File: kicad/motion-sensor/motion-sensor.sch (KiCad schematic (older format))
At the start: 21 parts, among them CON1 BARREL_JACK, IC1 ATMEGA328P-A, P1 ISP, P2 ESP8266, P3 CONN_01X03, P4 CONN_01X03, P5 CONN_01X02, Q1 Q_NMOS_DGS, SW1 Motion-Sensor-1, SW2 Motion-Sensor-2, U1 LM2574HVH-3.3

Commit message: added component lines + enclosure infos
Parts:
- added C1: 100nF, Capacitors_SMD:C_1206_HandSoldering, symbol C
- renumbered C3 to C2
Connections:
- net +3V3: now also C1.1
- net GND: now also C1.2
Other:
- note added: "Anschluss Bewegungsmelder"
- note added: "Mosfet Treiber für PWM"
- note added: "Status LED"
- note added: "Step Down Converter"
- moved on the sheet: D2, R3

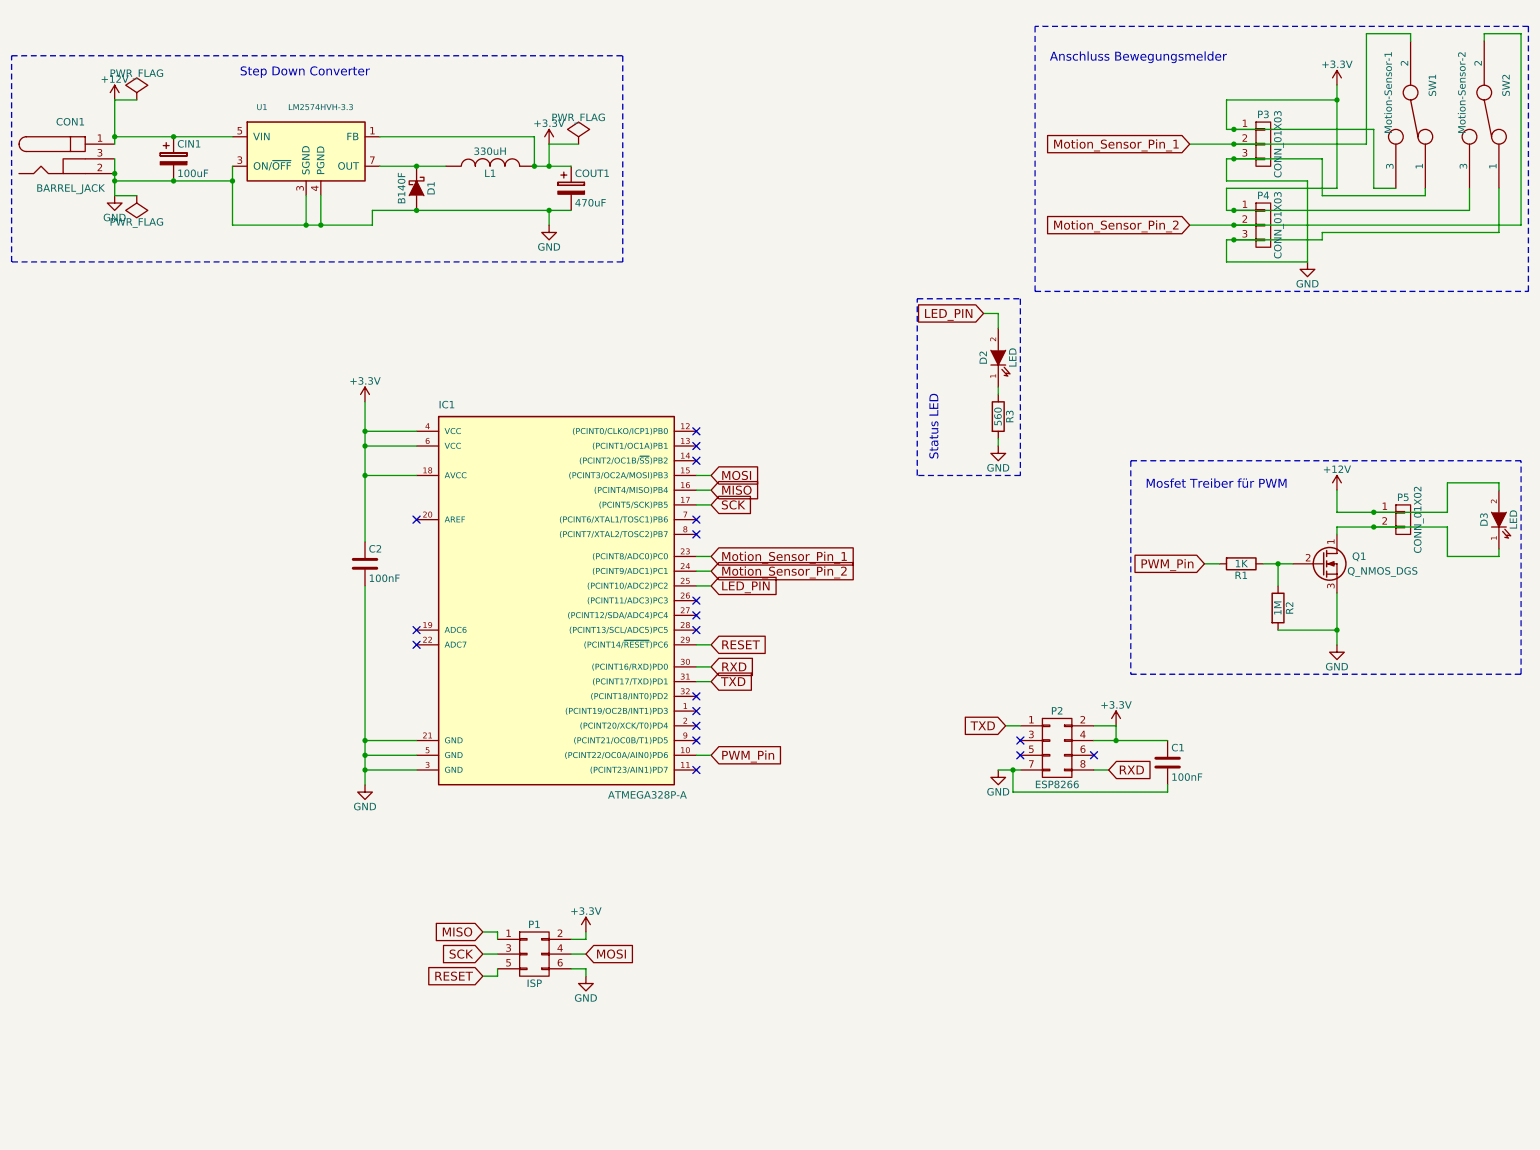
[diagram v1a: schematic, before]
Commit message: added custom footprints and finished schematic
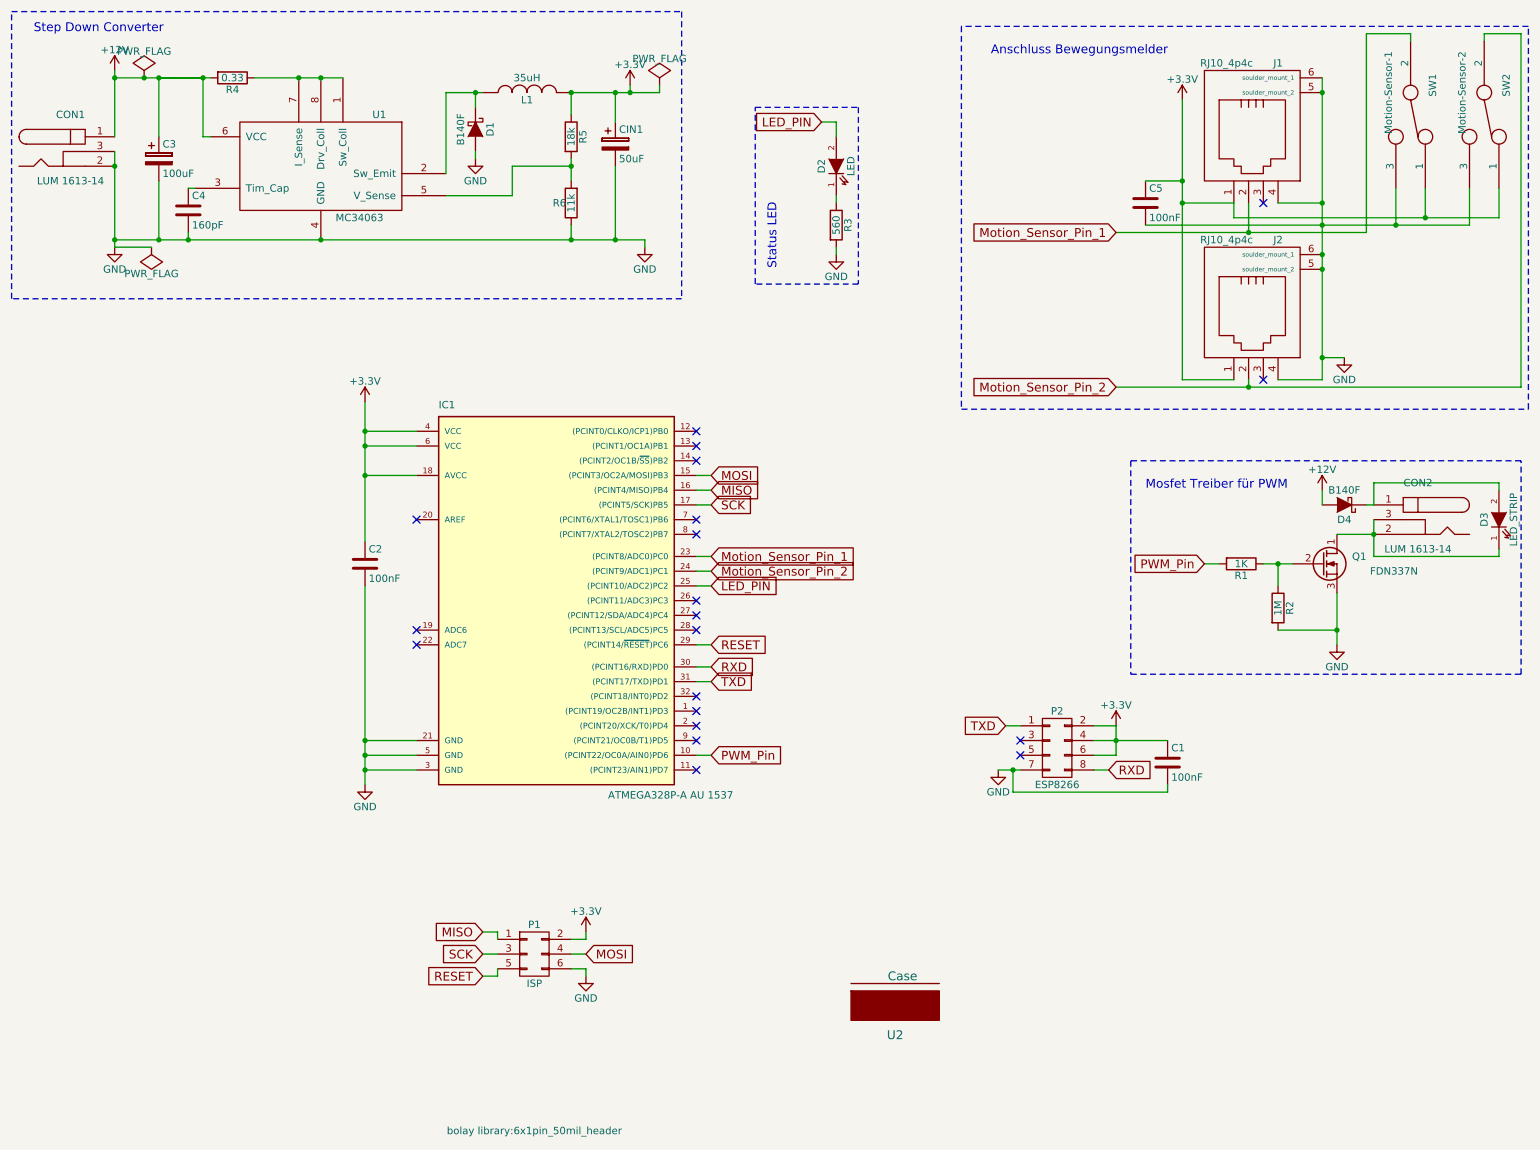
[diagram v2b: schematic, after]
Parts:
- removed P3, P4: CONN_01X03, symbol CONN_01X03
- removed P5: CONN_01X02, symbol CONN_01X02
- removed U1: LM2574HVH-3.3, symbol LM2574HVH-3.3
- added C4: 160pF, Capacitors_SMD:C_1206_HandSoldering, symbol C
- added C5: 100nF, Capacitors_SMD:C_1206_HandSoldering, symbol C
- added CON2: LUM 1613-14, bolay library:barrel_jack_ds_1613_14, symbol BARREL_JACK
- added D4: B140F, Diodes_SMD:DO-214AB_Handsoldering, symbol D_Schottky
- added J1, J2: RJ10_4p4c, bolay library:RJ10_SMD_4p4c, symbol RJ10_4p4c
- added R4: 0.33, Resistors_SMD:R_1206_HandSoldering, symbol R
- added R5: 18k, Resistors_SMD:R_1206_HandSoldering, symbol R
- added R6: 11k, Resistors_SMD:R_1206_HandSoldering, symbol R
- added U1: MC34063, SMD_Packages:SOIC-8-N, symbol MC34063-RESCUE-motion-sensor
- added U2: Case, symbol Case
- C1, C2: Digi-Key (none) -> 1276-2854-1-ND
- C3: renamed from COUT1; value 470uF -> 100uF; footprint Capacitors_SMD:c_elec_6.3x5.8 -> Capacitors_SMD:c_elec_6.3x7.7; Digi-Key (none) -> vorhanden
- CIN1: value 100uF -> 50uF; footprint Capacitors_SMD:c_elec_4x5.8 -> Capacitors_SMD:c_elec_6.3x7.7; Bemerkungen (none) -> 100uF Kondens von reichelt; Digi-Key (none) -> vorhanden
- CON1: value BARREL_JACK -> LUM 1613-14; footprint (none) -> bolay library:barrel_jack_ds_1613_14; Digi-Key (none) -> vorhanden
- D1: footprint (none) -> Diodes_SMD:DO-214AB_Handsoldering; Digi-Key (none) -> vorhanden
- D2: footprint (none) -> LEDs:LED-1206; Digi-Key (none) -> 160-1457-1-ND
- D3: value LED -> LED_STRIP; Digi-Key (none) -> vorhanden
- IC1: value ATMEGA328P-A -> ATMEGA328P-A AU 1537; footprint (none) -> Housings_QFP:TQFP-32_7x7mm_Pitch0.8mm; Digi-Key (none) -> vorhanden
- L1: value 330uH -> 35uH; footprint (none) -> bolay library:SRN_1060_Power_Inductors; Digi-Key (none) -> SRN1060-470MCT-ND
- P1: footprint (none) -> bolay library:6x1pin_50mil_header; Digi-Key (none) -> S9005E-06-ND
- P2: footprint (none) -> bolay library:8pin_Header_SMD; Digi-Key (none) -> S5674-ND
- Q1: value Q_NMOS_DGS -> FDN337N; footprint (none) -> TO_SOT_Packages_SMD:SOT-23_Handsoldering; Digi-Key (none) -> FDN337NTR-ND
- R1: footprint (none) -> Resistors_SMD:R_1206_HandSoldering; Digi-Key (none) -> 311-1.0KERCT-ND
- R2: footprint (none) -> Resistors_SMD:R_1206_HandSoldering; Digi-Key (none) -> 311-1.0MERCT-ND
- R3: footprint (none) -> Resistors_SMD:R_1206_HandSoldering; Digi-Key (none) -> 311-560ERCT-ND
- SW1, SW2: Digi-Key (none) -> vorhanden
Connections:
- net +12V: now also C3.1, D4.2 (A), R4.2, U1.6 (VCC); no longer CIN1.1, D3.2 (A)
- net +3V3: now also CIN1.1, P2.6 (P6), SW1.1, SW2.1, C5.1, J1.1, J2.1, R5.1; no longer C3.1, SW1.3, SW2.3
- net GND: now also SW1.3, SW2.3, C4.2, C5.2, J1.4, J1.5 (soulder_mount_2), J1.6 (soulder_mount_1), J2.4, J2.5 (soulder_mount_2), J2.6 (soulder_mount_1), R6.1, U1.4 (GND); no longer SW1.1, SW2.1
- net Motion_Sensor_Pin_1: now also J1.2
- net Motion_Sensor_Pin_2: now also J2.2
- net at D1.1 (K), L1.1: now also U1.2 (Sw_Emit)
- net at D3.1 (K), Q1.1 (D): now also CON2.2, CON2.3
- new net: CON2.1, D3.2 (A), D4.1 (K)
- new net: R4.1, U1.1 (Sw_Coll), U1.7 (I_Sense), U1.8 (Drv_Coll)
- new net: R5.2, R6.2, U1.5 (V_Sense)
- new net: C4.1, U1.3 (Tim_Cap)
- no-connect marks 19 -> 20
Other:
- moved on the sheet: C3, CIN1, CON1, D1, D2, L1, R3

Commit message: motion sensor project in kicad
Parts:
- added R7, R8, R9: 0, Resistors_SMD:R_1206_HandSoldering, symbol R
- D1: footprint Diodes_SMD:DO-214AB_Handsoldering -> Diodes_SMD:SMA_Handsoldering
- D2: footprint LEDs:LED-1206 -> LEDs:LED_1206
- D3: renamed from D4; footprint Diodes_SMD:DO-214AB_Handsoldering -> Diodes_SMD:SMA_Handsoldering
- U2: Digi-Key HM376-ND -> HM361-ND
- renumbered C3 to C1, C4 to C2, C2 to C3, C5 to C4, C1 to C5, D3 to D4, R4 to R1, R5 to R2, R6 to R3, R3 to R4, R1 to R5, R2 to R6
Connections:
- net +3V3: now also R7.1, R7.2
- net GND: now also R8.1, R8.2, R9.1, R9.2
- net Motion_Sensor_Pin_1: now also IC1.1 ((PCINT19/OC2B/INT1)PD3); no longer IC1.23 ((PCINT8/ADC0)PC0)
- net Motion_Sensor_Pin_2: now also IC1.32 ((PCINT18/INT0)PD2); no longer IC1.24 ((PCINT9/ADC1)PC1)
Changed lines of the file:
@@
 $EndComp
 $Comp
-L CP C3
+L CP C1
 U 1 1 56692A0A
 P 1500 1750
-F 0 "C3" H 1525 1850 50  0000 L CNN
+F 0 "C1" H 1525 1850 50  0000 L CNN
 F 1 "100uF" H 1525 1650 50  0000 L CNN
 F 2 "Capacitors_SMD:c_elec_6.3x7.7" H 1538 1600 50  0001 C CNN
@@
 F 0 "D1" H 3650 1650 50  0000 C CNN
 F 1 "B140F" H 3650 1450 50  0000 C CNN
-F 2 "Diodes_SMD:DO-214AB_Handsoldering" H 3650 1550 50  0001 C CNN
+F 2 "Diodes_SMD:SMA_Handsoldering" H 3650 1550 50  0001 C CNN
 F 3 "http://cdn-reichelt.de/documents/datenblatt/A400/B120-B160.pdf" H 3650 1550 50  0001 C CNN
 F 4 "vorhanden" H 3650 1550 60  0001 C CNN "Digi-Key"
@@
 $EndComp
 $Comp
-L C C2
+L C C3
 U 1 1 566944E6
 P 2900 4500
-F 0 "C2" H 2925 4600 50  0000 L CNN
+F 0 "C3" H 2925 4600 50  0000 L CNN
 F 1 "100nF" H 2925 4400 50  0000 L CNN
 F 2 "Capacitors_SMD:C_1206_HandSoldering" H 2938 4350 50  0001 C CNN
@@
 $EndComp
 $Comp
-L R R1
+L R R5
 U 1 1 56694619
 P 8850 4500
-F 0 "R1" V 8930 4500 50  0000 C CNN
+F 0 "R5" V 8930 4500 50  0000 C CNN
 F 1 "1K" V 8850 4500 50  0000 C CNN
 F 2 "Resistors_SMD:R_1206_HandSoldering" V 8780 4500 50  0001 C CNN
@@
 $EndComp
 $Comp
-L R R2
+L R R6
 U 1 1 56694914
 P 9100 4800
-F 0 "R2" V 9180 4800 50  0000 C CNN
+F 0 "R6" V 9180 4800 50  0000 C CNN
 F 1 "1M" V 9100 4800 50  0000 C CNN
 F 2 "Resistors_SMD:R_1206_HandSoldering" V 9030 4800 50  0001 C CNN
@@
 $EndComp
 $Comp
-L LED D3
+L LED D4
 U 1 1 566AD052
 P 10600 4200
-F 0 "D3" H 10600 4300 50  0000 C CNN
+F 0 "D4" H 10600 4300 50  0000 C CNN
 F 1 "LED_STRIP" H 10600 4100 50  0000 C CNN
 F 2 "" H 10600 4200 50  0000 C CNN
@@
 Text GLabel 8000 3300 0    60   Input ~ 0
 Motion_Sensor_Pin_2
-Text GLabel 5250 4450 2    60   Input ~ 0
+Text GLabel 5250 5500 2    60   Input ~ 0
 Motion_Sensor_Pin_1
-Text GLabel 5250 4550 2    60   Input ~ 0
+Text GLabel 5250 5400 2    60   Input ~ 0
 Motion_Sensor_Pin_2
 Text GLabel 8600 4500 0    60   Input ~ 0
@@
 F 0 "D2" H 6100 1900 50  0000 C CNN
 F 1 "LED" H 6100 1700 50  0000 C CNN
-F 2 "LEDs:LED-1206" H 6100 1800 50  0001 C CNN
+F 2 "LEDs:LED_1206" H 6100 1800 50  0001 C CNN
 F 3 "http://optoelectronics.liteon.com/upload/download/DS22-2000-253/S_110_LTST-C230KRKT.pdf" H 6100 1800 50  0001 C CNN
 F 4 "160-1457-1-ND" H 6100 1800 60  0001 C CNN "Digi-Key"
@@
 $EndComp
 $Comp
-L R R3
+L R R4
 U 1 1 566B38A0
 P 6100 2200
-F 0 "R3" V 6180 2200 50  0000 C CNN
+F 0 "R4" V 6180 2200 50  0000 C CNN
 F 1 "560" V 6100 2200 50  0000 C CNN
 F 2 "Resistors_SMD:R_1206_HandSoldering" V 6030 2200 50  0001 C CNN
@@
 NoConn ~ 5150 5700
 NoConn ~ 5150 5600
-NoConn ~ 5150 5500
-NoConn ~ 5150 5400
 NoConn ~ 5150 4950
 NoConn ~ 5150 4850
@@
 $EndComp
 $Comp
-L C C1
+L C C5
 U 1 1 566C9FBD
 P 8350 5850
-F 0 "C1" H 8375 5950 50  0000 L CNN
+F 0 "C5" H 8375 5950 50  0000 L CNN
 F 1 "100nF" H 8375 5750 50  0000 L CNN
 F 2 "Capacitors_SMD:C_1206_HandSoldering" H 8388 5700 50  0001 C CNN
@@
 $EndComp
 $Comp
-L R R4
+L R R1
 U 1 1 566F1004
 P 2000 1200
-F 0 "R4" V 2080 1200 50  0000 C CNN
+F 0 "R1" V 2080 1200 50  0000 C CNN
 F 1 "0.33" V 2000 1200 50  0000 C CNN
 F 2 "Resistors_SMD:R_1206_HandSoldering" V 1930 1200 50  0001 C CNN
@@
 $EndComp
 $Comp
-L R R5
+L R R2
 U 1 1 566F132C
 P 4300 1600
-F 0 "R5" V 4380 1600 50  0000 C CNN
+F 0 "R2" V 4380 1600 50  0000 C CNN
 F 1 "18k" V 4300 1600 50  0000 C CNN
 F 2 "Resistors_SMD:R_1206_HandSoldering" H 4230 1600 50  0001 C CNN
@@
 $EndComp
 $Comp
-L R R6
+L R R3
 U 1 1 566F13A6
 P 4300 2050
-F 0 "R6" H 4380 2050 50  0000 C CNN
+F 0 "R3" H 4380 2050 50  0000 C CNN
 F 1 "11k" V 4300 2050 50  0000 C CNN
 F 2 "Resistors_SMD:R_1206_HandSoldering" H 4230 2050 50  0001 C CNN
@@
 	8700 4500 8600 4500
 Wire Wire Line
-	5250 4550 5150 4550
-Wire Wire Line
-	5250 4450 5150 4450
-Wire Wire Line
 	3800 7300 3700 7300
 Wire Wire Line
@@
 	4300 1300 4900 1300
 $Comp
-L C C4
+L C C2
 U 1 1 566F646F
 P 1700 2100
-F 0 "C4" H 1725 2200 50  0000 L CNN
+F 0 "C2" H 1725 2200 50  0000 L CNN
 F 1 "160pF" H 1725 2000 50  0000 L CNN
 F 2 "Capacitors_SMD:C_1206_HandSoldering" H 1738 1950 50  0001 C CNN
@@
 $EndComp
 $Comp
-L C C5
+L C C4
 U 1 1 5671D8BE
 P 8200 2050
-F 0 "C5" H 8225 2150 50  0000 L CNN
+F 0 "C4" H 8225 2150 50  0000 L CNN
 F 1 "100nF" H 8225 1950 50  0000 L CNN
 F 2 "Capacitors_SMD:C_1206_HandSoldering" H 8238 1900 50  0001 C CNN
@@
 Wire Wire Line
 	8000 5800 7850 5800
-$Comp
-L RJ10_4p4c J2
-U 1 1 5680F36B
-P 8900 2800
-F 0 "J2" H 9100 3300 50  0000 C CNN
-F 1 "RJ10_4p4c" H 8750 3300 50  0000 C CNN
-F 2 "bolay library:RJ10_SMD_4p4c" H 8900 2800 50  0001 C CNN
-F 3 "http://portal.fciconnect.com/Comergent//fci/drawing/73306.pdf" H 8900 2800 50  0001 C CNN
-F 4 "609-4469-1-ND" H 8900 2800 60  0001 C CNN "Digi-Key"
-	1    8900 2800
-	1    0    0    -1
-$EndComp
-$Comp
-L RJ10_4p4c J1
-U 1 1 5680F75E
-P 8900 1600
-F 0 "J1" H 9100 2100 50  0000 C CNN
-F 1 "RJ10_4p4c" H 8750 2100 50  0000 C CNN
-F 2 "bolay library:RJ10_SMD_4p4c" H 8900 1600 50  0001 C CNN
-F 3 "http://portal.fciconnect.com/Comergent//fci/drawing/73306.pdf" H 8900 1600 50  0001 C CNN
-F 4 "609-4469-1-ND" H 8900 1600 60  0001 C CNN "Digi-Key"
-	1    8900 1600
-	1    0    0    -1
-$EndComp
 Wire Wire Line
 	9400 1200 9400 3250
@@
 Connection ~ 9750 4300
 $Comp
-L D_Schottky D4
+L D_Schottky D3
 U 1 1 5682436C
 P 9550 4100
-F 0 "D4" H 9550 4200 50  0000 C CNN
+F 0 "D3" H 9550 4200 50  0000 C CNN
 F 1 "B140F" H 9550 4000 50  0000 C CNN
-F 2 "Diodes_SMD:DO-214AB_Handsoldering" H 9550 4100 50  0001 C CNN
+F 2 "Diodes_SMD:SMA_Handsoldering" H 9550 4100 50  0001 C CNN
 F 3 "http://cdn-reichelt.de/documents/datenblatt/A400/B120-B160.pdf" H 9550 4100 50  0001 C CNN
 F 4 "vorhanden" H 9550 4100 60  0001 C CNN "Digi-Key"
@@
 F 2 "" H 6500 7500 60  0000 C CNN
 F 3 "http://www.hammondmfg.com/pdf/1551H.pdf" H 6500 7500 60  0001 C CNN
-F 4 "HM376-ND" H 6500 7500 60  0001 C CNN "Digi-Key"
+F 4 "HM361-ND" H 6500 7500 60  0001 C CNN "Digi-Key"
 	1    6500 7500
 	1    0    0    -1
 $EndComp
+$Comp
+L RJ10_4p4c J2
+U 1 1 56912E30
+P 8900 2800
+F 0 "J2" H 9100 3300 50  0000 C CNN
+F 1 "RJ10_4p4c" H 8750 3300 50  0000 C CNN
+F 2 "bolay library:RJ10_SMD_4p4c" H 8900 2800 50  0001 C CNN
+F 3 "http://portal.fciconnect.com/Comergent//fci/drawing/73306.pdf" H 8900 2800 50  0001 C CNN
+F 4 "609-4469-1-ND" H 8900 2800 60  0001 C CNN "Digi-Key"
+	1    8900 2800
+	1    0    0    -1
+$EndComp
+$Comp
+L RJ10_4p4c J1
+U 1 1 5691303D
+P 8900 1600
+F 0 "J1" H 9100 2100 50  0000 C CNN
+F 1 "RJ10_4p4c" H 8750 2100 50  0000 C CNN
+F 2 "bolay library:RJ10_SMD_4p4c" H 8900 1600 50  0001 C CNN
+F 3 "http://portal.fciconnect.com/Comergent//fci/drawing/73306.pdf" H 8900 1600 50  0001 C CNN
+F 4 "609-4469-1-ND" H 8900 1600 60  0001 C CNN "Digi-Key"
+	1    8900 1600
+	1    0    0    -1
+$EndComp
+Wire Wire Line
+	5150 5400 5250 5400
+Wire Wire Line
+	5150 5500 5250 5500
+NoConn ~ 5150 4450
+NoConn ~ 5150 4550
+$Comp
+L +3.3V #PWR020
+U 1 1 56B23B4C
+P 1850 3400
+F 0 "#PWR020" H 1850 3250 50  0001 C CNN
+F 1 "+3.3V" H 1850 3540 50  0000 C CNN
+F 2 "" H 1850 3400 50  0000 C CNN
+F 3 "" H 1850 3400 50  0000 C CNN
+	1    1850 3400
+	1    0    0    -1
+$EndComp
+$Comp
+L +3.3V #PWR021
+U 1 1 56B23BAE
+P 2250 3400
+F 0 "#PWR021" H 2250 3250 50  0001 C CNN
+F 1 "+3.3V" H 2250 3540 50  0000 C CNN
+F 2 "" H 2250 3400 50  0000 C CNN
+F 3 "" H 2250 3400 50  0000 C CNN
+	1    2250 3400
+	1    0    0    -1
+$EndComp
+$Comp
+L GND #PWR022
+U 1 1 56B23D32
+P 1850 4150
+F 0 "#PWR022" H 1850 3900 50  0001 C CNN
+F 1 "GND" H 1850 4000 50  0000 C CNN
+F 2 "" H 1850 4150 50  0000 C CNN
+F 3 "" H 1850 4150 50  0000 C CNN
+	1    1850 4150
+	1    0    0    -1
+$EndComp
+$Comp
+L GND #PWR023
+U 1 1 56B23D94
+P 2250 4150
+F 0 "#PWR023" H 2250 3900 50  0001 C CNN
+F 1 "GND" H 2250 4000 50  0000 C CNN
+F 2 "" H 2250 4150 50  0000 C CNN
+F 3 "" H 2250 4150 50  0000 C CNN
+	1    2250 4150
+	1    0    0    -1
+$EndComp
+$Comp
+L R R7
+U 1 1 56B23ECF
+P 2050 3500
+F 0 "R7" V 2130 3500 50  0000 C CNN
+F 1 "0" V 2050 3500 50  0000 C CNN
+F 2 "Resistors_SMD:R_1206_HandSoldering" V 1980 3500 50  0001 C CNN
+F 3 "http://www.yageo.com.tw/exep/pages/download/literatures/PYu-R_INT-thick_7.pdf" H 2050 3500 50  0001 C CNN
+F 4 "311-0.0ERCT-ND" H 2050 3500 60  0001 C CNN "Digi-Key"
+	1    2050 3500
+	0    1    1    0
+$EndComp
+Wire Wire Line
+	1850 3400 1850 3500
+Wire Wire Line
+	1850 3500 1900 3500
+Wire Wire Line
+	2200 3500 2250 3500
+Wire Wire Line
+	2250 3500 2250 3400
+Wire Wire Line
+	2250 3900 2250 4150
+Wire Wire Line
+	2250 4050 2200 4050
+Wire Wire Line
+	1900 4050 1850 4050
+Wire Wire Line
+	1850 3900 1850 4150
+$Comp
+L R R8
+U 1 1 56B243CB
+P 2050 4050
+F 0 "R8" V 2130 4050 50  0000 C CNN
+F 1 "0" V 2050 4050 50  0000 C CNN
+F 2 "Resistors_SMD:R_1206_HandSoldering" V 1980 4050 50  0001 C CNN
+F 3 "http://www.yageo.com.tw/exep/pages/download/literatures/PYu-R_INT-thick_7.pdf" H 2050 4050 50  0001 C CNN
+F 4 "311-0.0ERCT-ND" H 2050 4050 60  0001 C CNN "Digi-Key"
+	1    2050 4050
+	0    1    1    0
+$EndComp
+$Comp
+L R R9
+U 1 1 56B24DF4
+P 2050 3900
+F 0 "R9" V 2130 3900 50  0000 C CNN
+F 1 "0" V 2050 3900 50  0000 C CNN
+F 2 "Resistors_SMD:R_1206_HandSoldering" V 1980 3900 50  0001 C CNN
+F 3 "http://www.yageo.com.tw/exep/pages/download/literatures/PYu-R_INT-thick_7.pdf" H 2050 3900 50  0001 C CNN
+F 4 "311-0.0ERCT-ND" H 2050 3900 60  0001 C CNN "Digi-Key"
+	1    2050 3900
+	0    1    1    0
+$EndComp
+Wire Wire Line
+	2200 3900 2250 3900
+Connection ~ 2250 4050
+Wire Wire Line
+	1900 3900 1850 3900
+Connection ~ 1850 4050
 $EndSCHEMATC
